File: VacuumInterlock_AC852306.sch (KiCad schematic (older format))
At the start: 0 parts

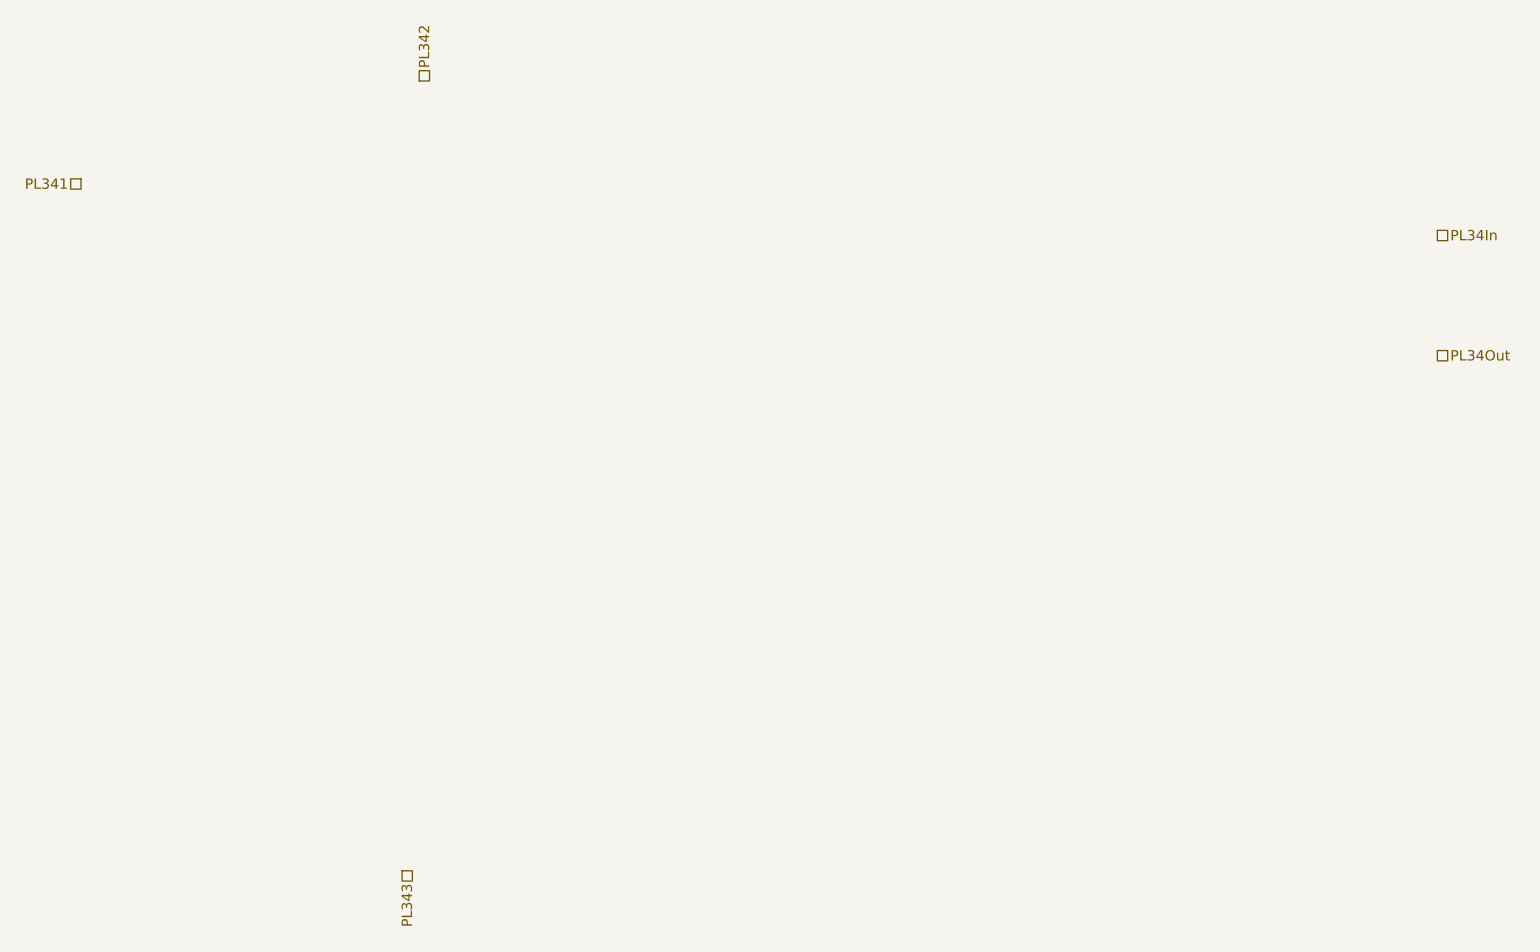
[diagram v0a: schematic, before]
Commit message: added ColumnWiring, DataSystemAutoReset, KVSelection and VacuumInterlock
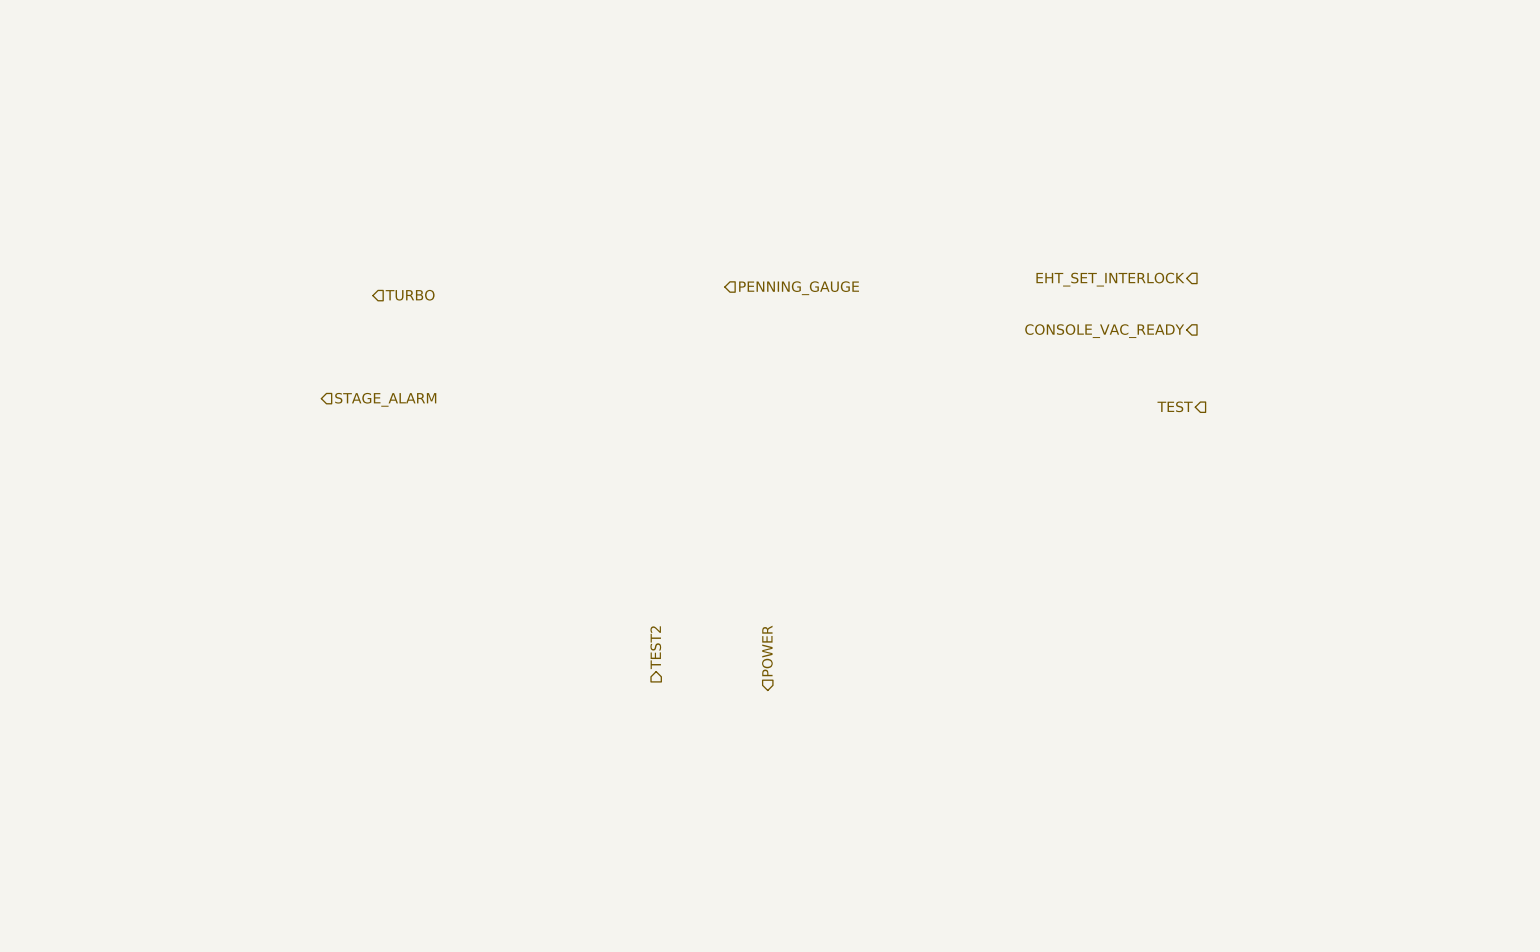
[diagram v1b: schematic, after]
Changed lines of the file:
@@
 $Descr A4 11693 8268
 encoding utf-8
-Sheet 9 25
+Sheet 25 25
 Title ""
 Date ""
@@
 Comment4 ""
 $EndDescr
-Text HLabel 1800 1900 0    60   UnSpc ~ 0
-PL341
-Text HLabel 3800 1300 1    60   UnSpc ~ 0
-PL342
-Text HLabel 3700 5900 3    60   UnSpc ~ 0
-PL343
-Text HLabel 9700 2200 2    60   UnSpc ~ 0
-PL34In
-Text HLabel 9700 2900 2    60   UnSpc ~ 0
-PL34Out
+Text HLabel 8300 2450 0    60   Output ~ 0
+EHT_SET_INTERLOCK
+Text HLabel 8300 2750 0    60   Output ~ 0
+CONSOLE_VAC_READY
+Text HLabel 8350 3200 0    60   Output ~ 0
+TEST
+Text HLabel 5150 4800 1    60   Output ~ 0
+TEST2
+Text HLabel 5800 4850 1    60   Input ~ 0
+POWER
+Text HLabel 5550 2500 2    60   Input ~ 0
+PENNING_GAUGE
+Text HLabel 3500 2550 2    60   Input ~ 0
+TURBO
+Text HLabel 3200 3150 2    60   Input ~ 0
+STAGE_ALARM
 $EndSCHEMATC
